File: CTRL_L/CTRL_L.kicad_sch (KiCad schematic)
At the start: 29 parts, among them J1 503480-0540, J2 AYF530365TA, J3 5034801400, J6 AYF530365TA, U1 74LVC1G08, U2 DRV5033FAxDBZ

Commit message: Updated CTRL_L to use 4 pin FPC (3 pin is hard to source!)
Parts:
- removed J6: AYF530365TA, AYF530365TA:AYF530365T, symbol AYF530365TA:AYF530365TA
- added J4: 503480-0440, 503480-0440:5034800440, symbol 503480-0440:503480-0440
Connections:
- net Col1: now also J4.3
- net Col2: now also J4.1
- net GND: now also J4.4, J4.MP1, J4.MP2
- net Row1: now also J4.2
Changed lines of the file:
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@@
+	)
+	(symbol
+		(lib_id "power:GND")
+		(at 80.01 119.38 90)
+		(unit 1)
+		(body_style 1)
+		(exclude_from_sim no)
+		(in_bom yes)
+		(on_board yes)
+		(in_pos_files yes)
+		(dnp no)
+		(fields_autoplaced yes)
+		(property "Reference" "#PWR033"
+			(at 86.36 119.38 0)
+			(hide yes)
+			(show_name no)
+			(do_not_autoplace no)
+			(effects
+				(font
+					(size 1.27 1.27)
+				)
+			)
+		)
+		(property "Value" "GND"
+			(at 83.82 119.3799 90)
+			(show_name no)
+			(do_not_autoplace no)
+			(effects
+				(font
+					(size 1.27 1.27)
+				)
+				(justify right)
+			)
+		)
+		(property "Footprint" ""
+			(at 80.01 119.38 0)
+			(hide yes)
+			(show_name no)
+			(do_not_autoplace no)
+			(effects
+				(font
+					(size 1.27 1.27)
+				)
+			)
+		)
+		(property "Datasheet" ""
+			(at 80.01 119.38 0)
+			(hide yes)
+			(show_name no)
+			(do_not_autoplace no)
+			(effects
+				(font
+					(size 1.27 1.27)
+				)
+			)
+		)
+		(property "Description" "Power symbol creates a global label with name \"GND\" , ground"
+			(at 80.01 119.38 0)
+			(hide yes)
+			(show_name no)
+			(do_not_autoplace no)
+			(effects
+				(font
+					(size 1.27 1.27)
+				)
+			)
+		)
+		(pin "1"
+		)
+		(instances
+			(project "CTRL_L"
+				(path "/8eeed083-de7a-4dfe-ba6c-9e042c3ef75c"
+					(reference "#PWR033")
+					(unit 1)
+				)
+			)
+		)
 	)
 	(symbol
@@
 	)
 	(symbol
-		(lib_id "AYF530365TA:AYF530365TA")
+		(lib_id "503480-0440:503480-0440")
 		(at 57.15 127 0)
 		(mirror x)
@@
 		(in_pos_files yes)
 		(dnp no)
-		(property "Reference" "J6"
+		(fields_autoplaced yes)
+		(property "Reference" "J4"
+			(at 68.58 111.76 0)
+			(show_name no)
+			(do_not_autoplace no)
+			(effects
+				(font
+					(size 1.27 1.27)
+				)
+			)
+		)
+		(property "Value" "503480-0440"
 			(at 68.58 114.3 0)
 			(show_name no)
@@
 			)
 		)
-		(property "Value" "AYF530365TA"
-			(at 68.58 116.84 0)
-			(show_name no)
-			(do_not_autoplace no)
-			(effects
-				(font
-					(size 1.27 1.27)
-				)
-			)
-		)
-		(property "Footprint" "AYF530365TA:AYF530365T"
+		(property "Footprint" "503480-0440:5034800440"
 			(at 76.2 32.08 0)
 			(hide yes)
@@
 			)
 		)
-		(property "Datasheet" "https://www3.panasonic.biz/ac/e_download/control/connector/fpc-ffc/catalog/con_eng_y5bw.pdf"
+		(property "Datasheet" "https://www.molex.com/pdm_docs/sd/5034800440_sd.pdf"
 			(at 76.2 -67.92 0)
 			(hide yes)
@@
 			)
 		)
-		(property "Description" "3 Position FPC Connector Contacts, Top and Bottom 0.020\" (0.50mm) Surface Mount, Right Angle"
+		(property "Description" "Connector FFC/FPC SKT 4 Position 0.5mm Solder Right Angle Surface Mount T/R"
 			(at 57.15 127 0)
 			(hide yes)
@@
 			)
 		)
-		(property "Height" "1.76"
+		(property "Height" "2.12"
 			(at 76.2 -267.92 0)
 			(hide yes)
@@
 			)
 		)
-		(property "Mouser Part Number" "667-AYF530365TA"
+		(property "Mouser Part Number" "538-503480-0440"
 			(at 76.2 -367.92 0)
 			(hide yes)
@@
 			)
 		)
-		(property "Mouser Price/Stock" "https://www.mouser.co.uk/ProductDetail/Panasonic-Industrial-Devices/AYF530365TA?qs=tY4uNICHPYl8dOyO14vLEA%3D%3D"
+		(property "Mouser Price/Stock" "https://www.mouser.co.uk/ProductDetail/Molex/503480-0440?qs=LBbezbu20sggwP%2FAt293Pw%3D%3D"
 			(at 76.2 -467.92 0)
 			(hide yes)
@@
 			)
 		)
-		(property "Manufacturer_Name" "Panasonic"
+		(property "Manufacturer_Name" "Molex"
 			(at 76.2 -567.92 0)
 			(hide yes)
@@
 			)
 		)
-		(property "Manufacturer_Part_Number" "AYF530365TA"
+		(property "Manufacturer_Part_Number" "503480-0440"
 			(at 76.2 -667.92 0)
 			(hide yes)
@@
 			)
 		)
+		(pin "4"
+		)
+		(pin "MP1"
+		)
 		(pin "3"
 		)
-		(pin "5"
-		)
 		(pin "2"
 		)
-		(pin "4"
+		(pin "MP2"
 		)
 		(pin "1"
@@
 			(project "CTRL_L"
 				(path "/8eeed083-de7a-4dfe-ba6c-9e042c3ef75c"
-					(reference "J6")
+					(reference "J4")
 					(unit 1)
 				)

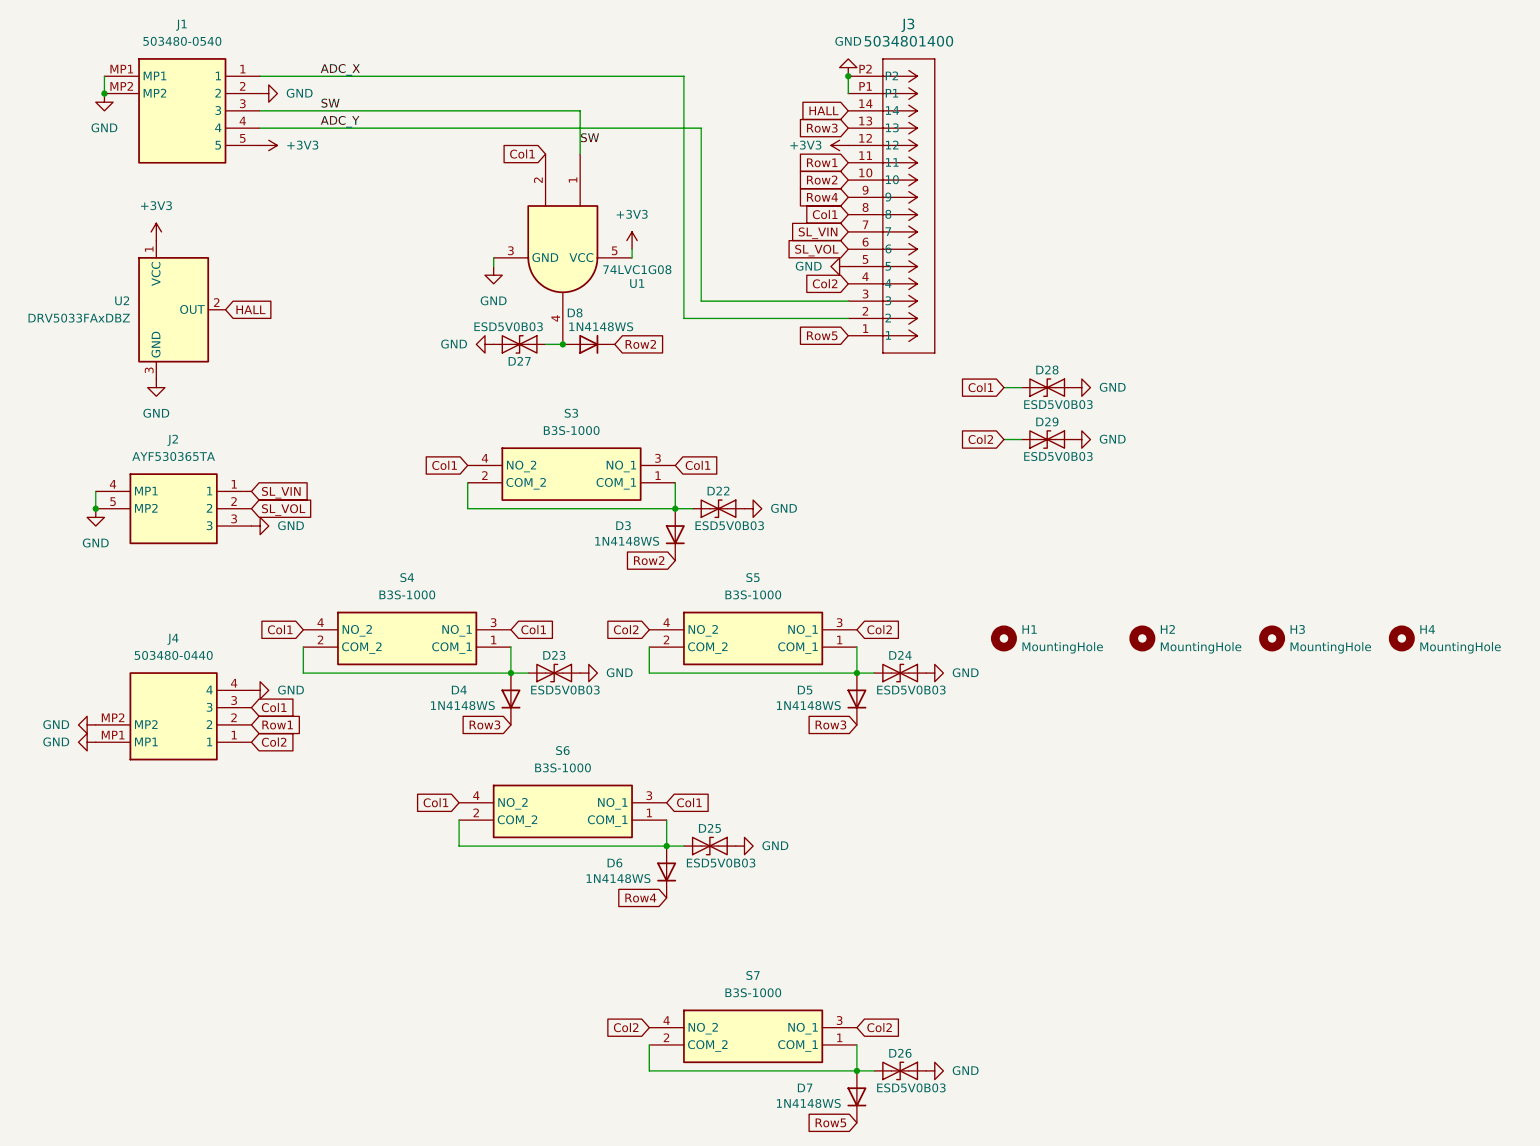
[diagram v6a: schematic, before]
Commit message: Updated CTRLs to be one sided (saves a billion dollars somehow), added LCSC_Parts for BOM, and other fixes. (Part 1/2)
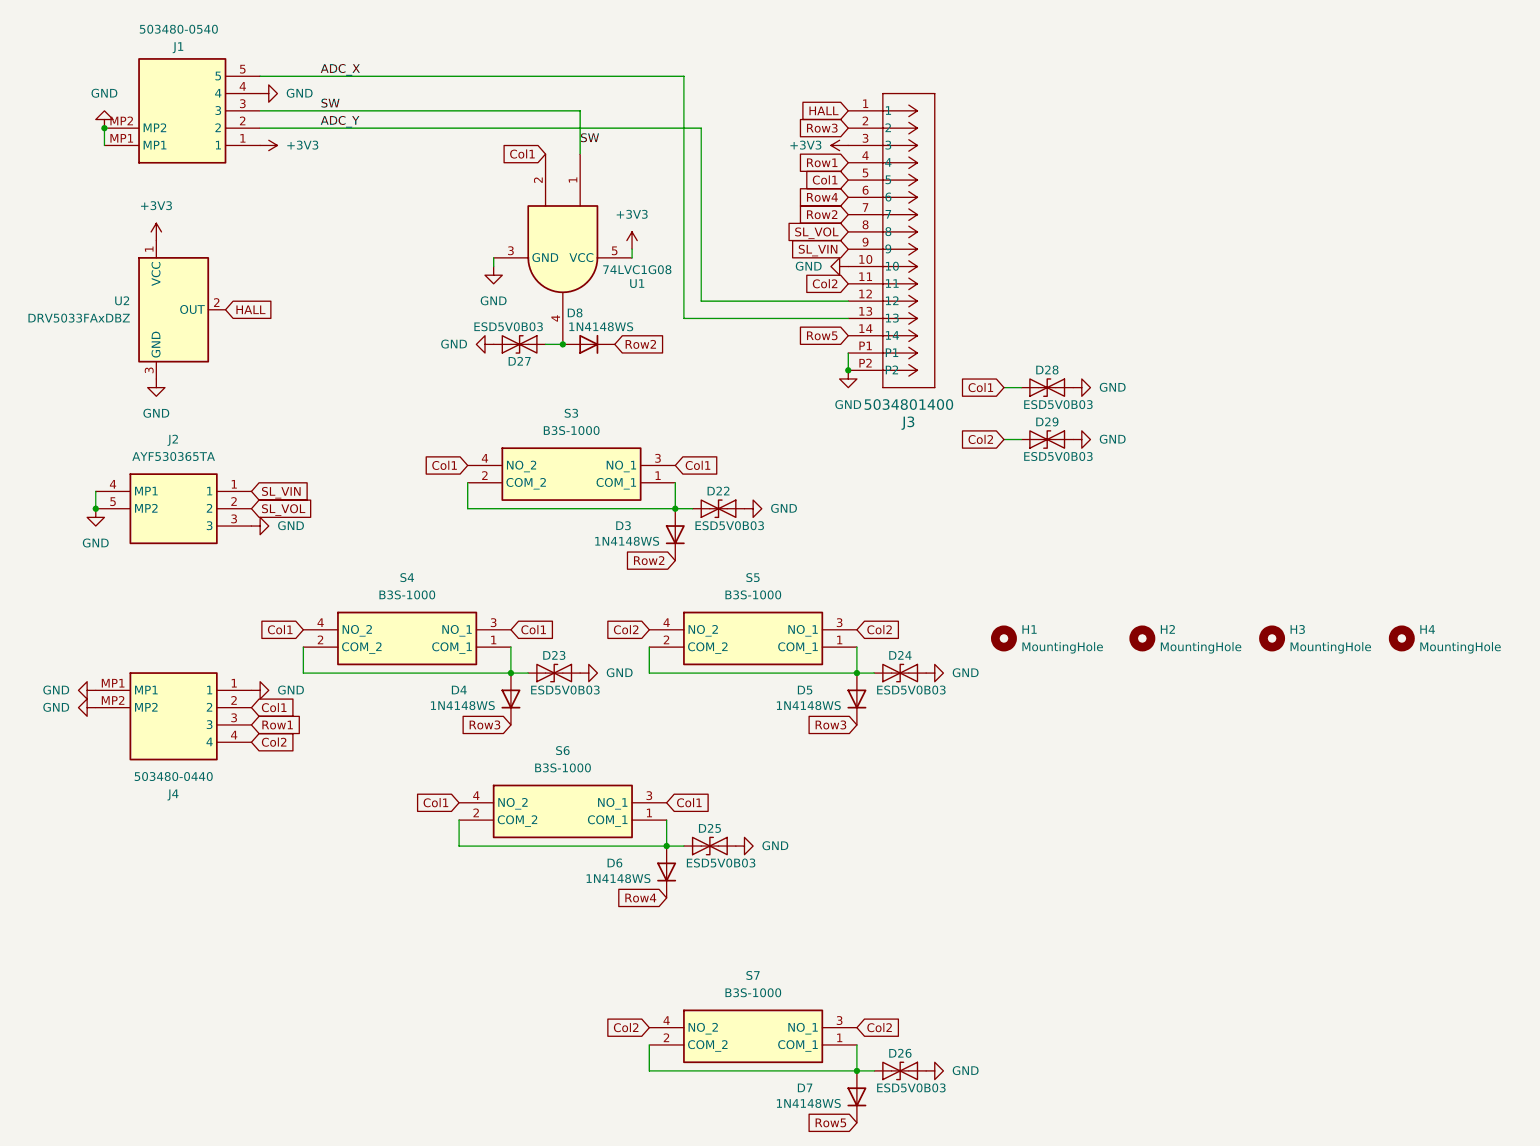
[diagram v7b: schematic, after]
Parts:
- D3, D4, D5, D6, D7, D8: LCSC Part (none) -> C917117
- H1, H2, H3, H4: LCSC Part (none) -> N/A
- J1: LCSC Part (none) -> C5527934
- J2: LCSC Part (none) -> C5571510
- J3: LCSC Part (none) -> C505360
- J4: LCSC Part (none) -> C3170007
- S3, S4, S5, S6, S7: LCSC Part (none) -> C2733655
- U1: LCSC Part (none) -> C53185136
- U2: LCSC Part (none) -> C2869057
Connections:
- net +3V3: now also J1.1, J3.3; no longer J1.5, J3.12
- net ADC_X: now also J1.5, J3.13; no longer J1.1, J3.2
- net ADC_Y: now also J1.2, J3.12; no longer J1.4, J3.3
- net Col1: now also J3.5, J4.2; no longer J3.8, J4.3
- net Col2: now also J3.11, J4.4; no longer J3.4, J4.1
- net GND: now also J1.4, J3.10, J4.1; no longer J1.2, J3.5, J4.4
- net HALL: now also J3.1; no longer J3.14
- net Row1: now also J3.4, J4.3; no longer J3.11, J4.2
- net Row2: now also J3.7; no longer J3.10
- net Row3: now also J3.2; no longer J3.13
- net Row4: now also J3.6; no longer J3.9
- net Row5: now also J3.14; no longer J3.1
- net SL_VIN: now also J3.9; no longer J3.7
- net SL_VOL: now also J3.8; no longer J3.6
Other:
- moved on the sheet: J3

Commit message: Created updated BOM for PCBWay on all CTRL daughterboards. These boards have likely hit their final* version
*Ive said "Finished Version" many times in this project. I'm confident now, but no guarantees.
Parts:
- D22, D23, D24, D25, D26, D27, D28, D29: MPN (none) -> ESD5V0B03-1006; Manufacturer (none) -> TECH PUBLIC
- D3, D4, D5, D6, D7, D8: MPN (none) -> 1N4148WS; Manufacturer (none) -> JSMSEMI
- J1: MPN (none) -> 5034800540; Manufacturer (none) -> MOLEX
- J2: MPN (none) -> AYF530365TA; Manufacturer (none) -> PANASONIC
- J3: MPN (none) -> 5034801400; Manufacturer (none) -> MOLEX
- J4: MPN (none) -> 5034800440; Manufacturer (none) -> MOLEX
- S3, S4, S5, S6, S7: MPN (none) -> B3S-1000; Manufacturer (none) -> OMRON
- U1: MPN (none) -> 74LVC1G08GV; Manufacturer (none) -> MDD(Microdiode Semiconductor)
- U2: MPN (none) -> DRV5033FAQDBZR; Manufacturer (none) -> TI
